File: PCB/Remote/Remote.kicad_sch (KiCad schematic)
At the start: 5 parts, among them J2 Joystick (Servo), J3 Joystick (Motor), SW2 Auto/Manual, SW3 Siren on/off, U6 NRF24L01

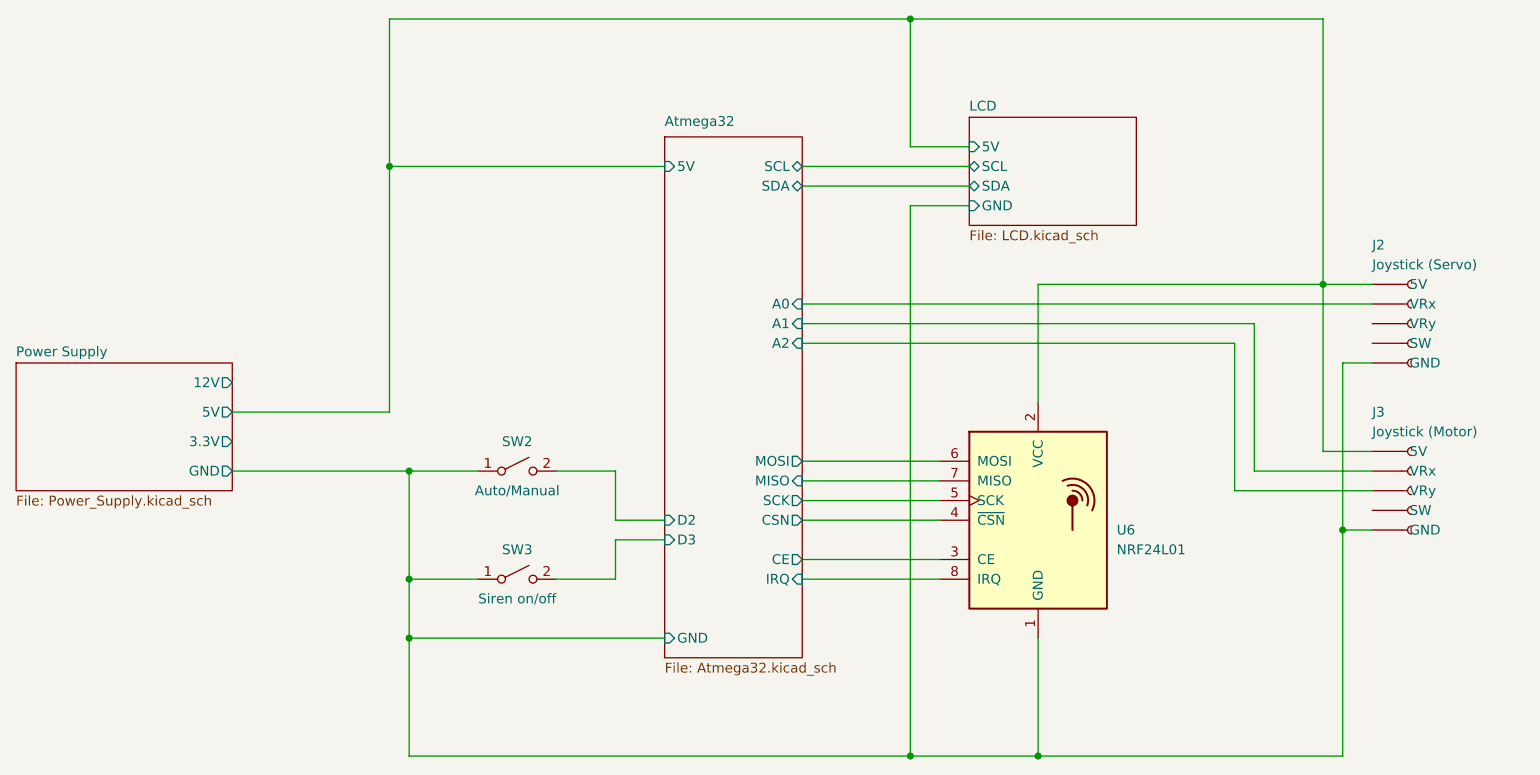
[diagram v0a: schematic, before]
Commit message: 3.3v error in PCB
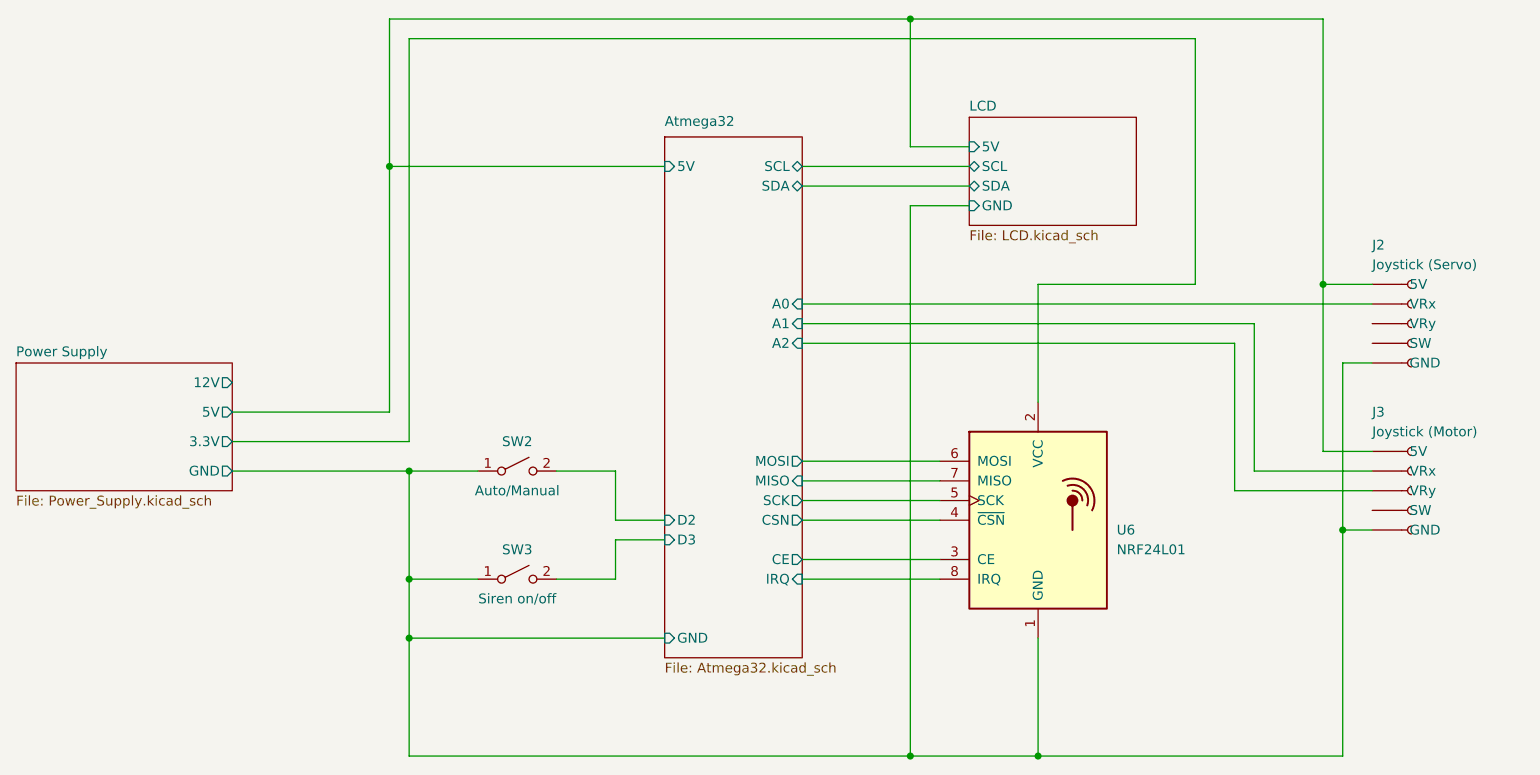
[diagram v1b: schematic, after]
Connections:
- net Atmega32/5V: no longer U6.2 (VCC)
- net Power Supply/3.3V: now also U6.2 (VCC)
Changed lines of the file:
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@@
+    (stroke (width 0) (type default) (color 0 0 0 0))
+  )
+  (wire (pts (xy 110.49 49.53) (xy 212.09 49.53))
+    (stroke (width 0) (type default) (color 0 0 0 0))
+  )
+  (wire (pts (xy 212.09 81.28) (xy 191.77 81.28))
     (stroke (width 0) (type default) (color 0 0 0 0))
   )
@@
   )
   (wire (pts (xy 219.71 105.41) (xy 219.71 86.36))
+    (stroke (width 0) (type default) (color 0 0 0 0))
+  )
+  (wire (pts (xy 110.49 101.6) (xy 110.49 49.53))
     (stroke (width 0) (type default) (color 0 0 0 0))
   )
@@
   )
   (wire (pts (xy 234.95 113.03) (xy 231.14 113.03))
+    (stroke (width 0) (type default) (color 0 0 0 0))
+  )
+  (wire (pts (xy 212.09 49.53) (xy 212.09 81.28))
     (stroke (width 0) (type default) (color 0 0 0 0))
   )
@@
     (stroke (width 0) (type default) (color 0 0 0 0))
   )
-  (wire (pts (xy 191.77 81.28) (xy 228.6 81.28))
-    (stroke (width 0) (type default) (color 0 0 0 0))
-  )
   (wire (pts (xy 110.49 142.24) (xy 110.49 127))
     (stroke (width 0) (type default) (color 0 0 0 0))
@@
     (stroke (width 0) (type default) (color 0 0 0 0))
   )
+  (wire (pts (xy 87.63 101.6) (xy 110.49 101.6))
+    (stroke (width 0) (type default) (color 0 0 0 0))
+  )
